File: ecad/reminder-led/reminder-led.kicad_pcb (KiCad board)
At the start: 2 copper layers, 13 parts, among them J1 MOLEX SL 1x5, Q1 2N3904, Q2 2N3904, Q3 2N3904

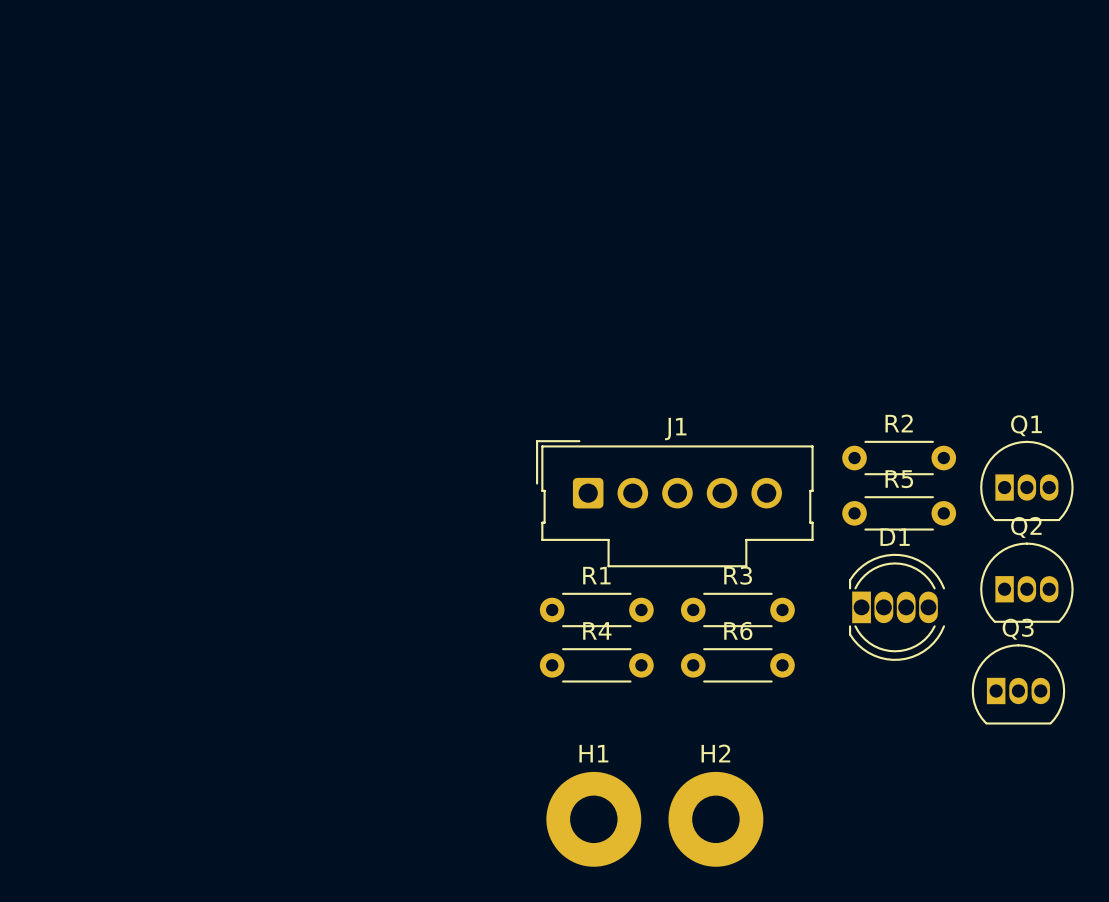
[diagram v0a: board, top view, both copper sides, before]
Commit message: Changed LED board type to 5050 LED
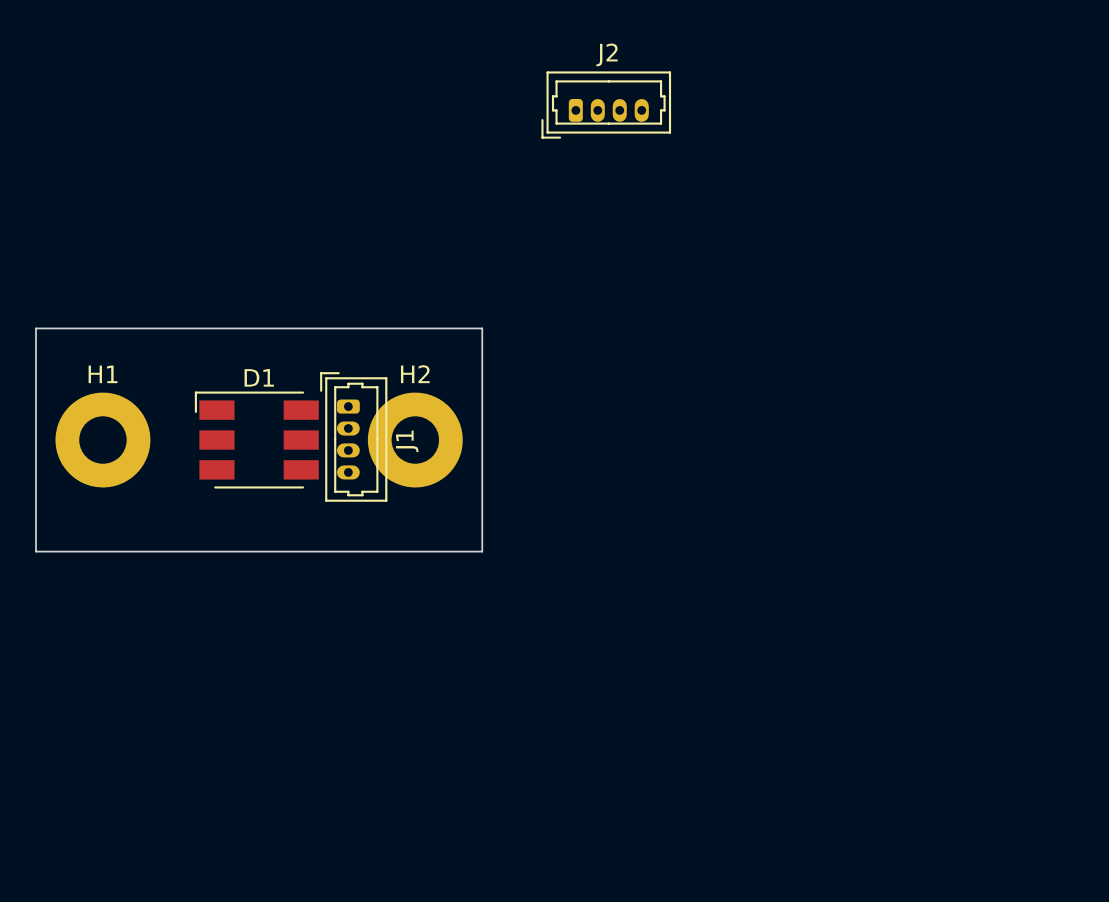
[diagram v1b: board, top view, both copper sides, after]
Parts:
- removed Q1, Q2, Q3: 2N3904, Package_TO_SOT_THT:TO-92_Inline
- removed R1, R2, R3: 620, Resistor_THT:R_Axial_DIN0204_L3.6mm_D1.6mm_P5.08mm_Horizontal
- removed R4: 130, Resistor_THT:R_Axial_DIN0204_L3.6mm_D1.6mm_P5.08mm_Horizontal
- removed R5, R6: 91, Resistor_THT:R_Axial_DIN0204_L3.6mm_D1.6mm_P5.08mm_Horizontal
- added J2: 0530470410, Connector_Molex:Molex_PicoBlade_53047-0410_1x04_P1.25mm_Vertical, F.Cu at (151.4, 70.1)
- D1: value LED_RGBA -> APA102; footprint LED_THT:LED_D5.0mm-4_RGB -> LED_SMD:LED_RGB_5050-6
- J1: value MOLEX SL 1x5 -> 0530470410; footprint Connector_Molex:Molex_SL_171971-0005_1x05_P2.54mm_Vertical -> Connector_Molex:Molex_PicoBlade_53047-0410_1x04_P1.25mm_Vertical
- moved D1 35.6 mm to (133.3, 88.9)
- moved H1 35.3 mm to (124.5, 88.9)
- moved H2 27.5 mm to (142.2, 88.9)
- moved J1 14.5 mm to (138.4, 87.0), turned to 270 degrees
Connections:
- D1 pad 1: Net-(D1-Pad1) -> /SER_IN
- D1 pad 2: Net-(D1-Pad2) -> /CLK_IN
- D1 pad 3: Net-(D1-Pad3) -> GND
- J1 pad 2: /LED_R -> /SER_IN
- J1 pad 3: /LED_G -> /CLK_IN
- J1 pad 4: /LED_B -> GND
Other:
- board outline added: 25.4 x 12.7 mm

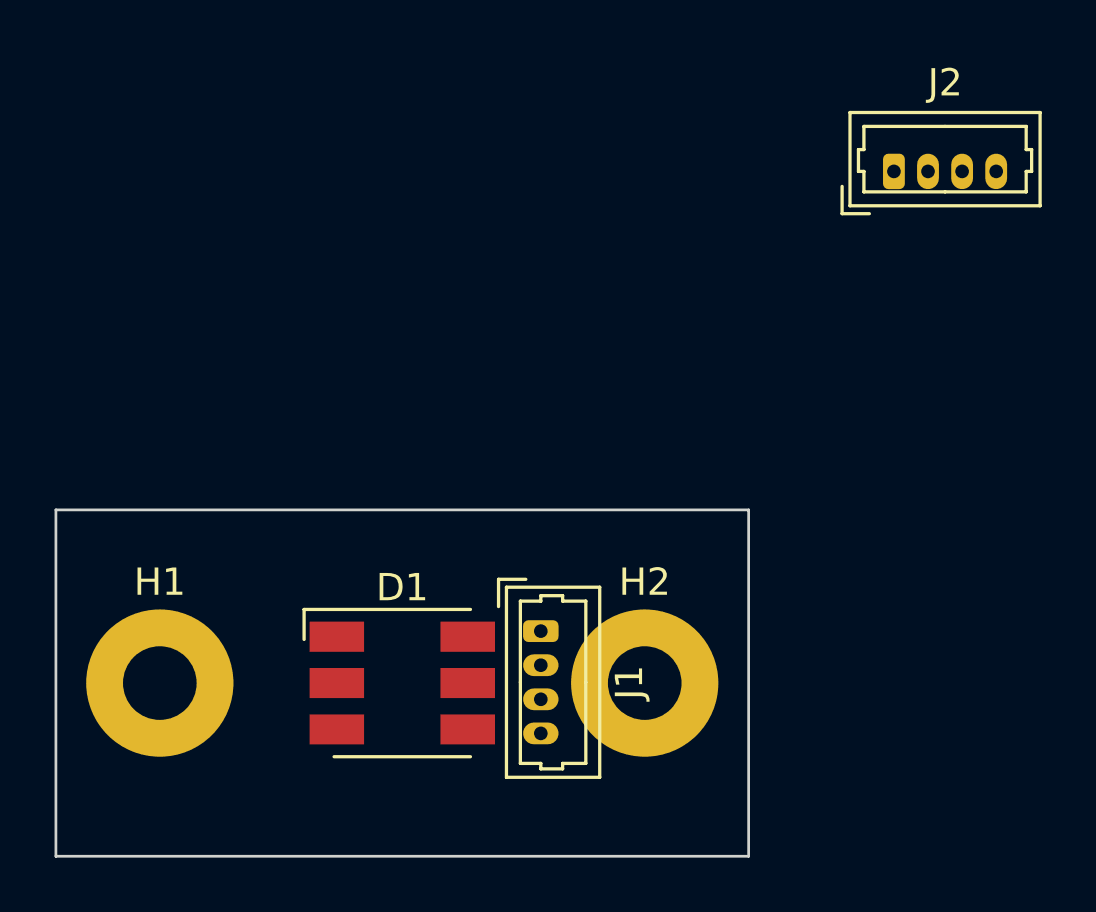
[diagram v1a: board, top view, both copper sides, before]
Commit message: Finished LED board routing and detailing
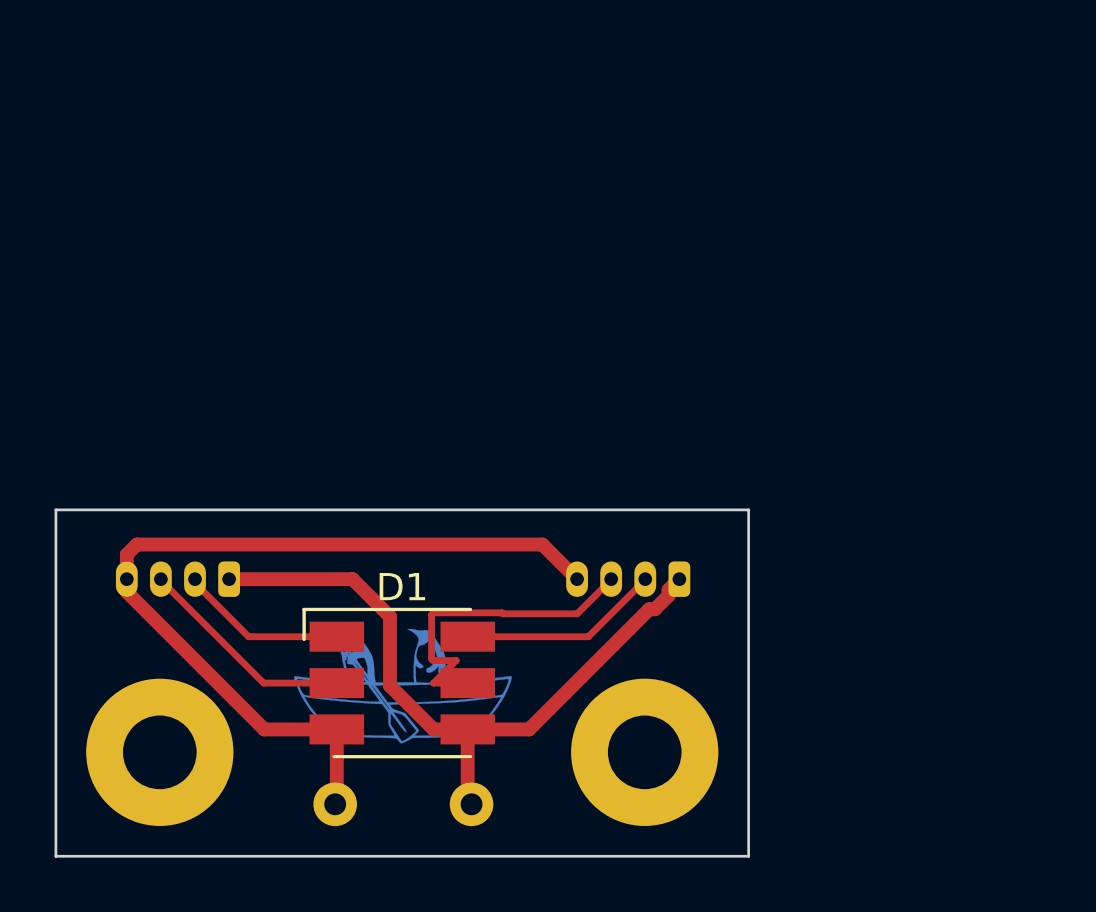
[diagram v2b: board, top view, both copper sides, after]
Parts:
- added C1: 10uF 10V, Capacitor_THT:C_Rect_L7.0mm_W2.0mm_P5.00mm, B.Cu at (135.9, 93.3)
- added G***: LOGO, Decals:8mm-penguin, B.Cu at (133.3, 88.9)
- J1, J2: moved to B.Cu
- moved J2 16.9 mm to (143.5, 85.1), turned to 180 degrees
- moved J1 11.6 mm to (127.0, 85.1), turned to 180 degrees
- moved H1 2.54 mm to (124.5, 91.4)
- moved H2 2.54 mm to (142.2, 91.4)
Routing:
- net GND: track 0.00 -> 31.1 mm
- net +5V: track 0.00 -> 25.5 mm
- net /CLK_OUT: track 0.00 -> 12.1 mm
- net /CLK_IN: track 0.00 -> 8.05 mm
- net /SER_OUT: track 0.00 -> 7.40 mm
- net /SER_IN: track 0.00 -> 6.16 mm
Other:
- board text added: "5V SER CLK GND"
- board text added: "IN"
- board text added: "OUT"

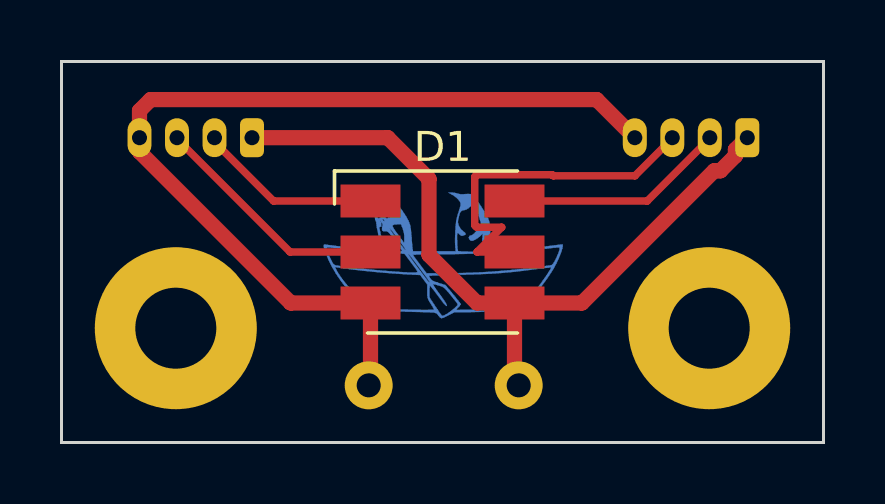
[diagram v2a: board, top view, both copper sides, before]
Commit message: Added rev text and chamfered corners of PCB
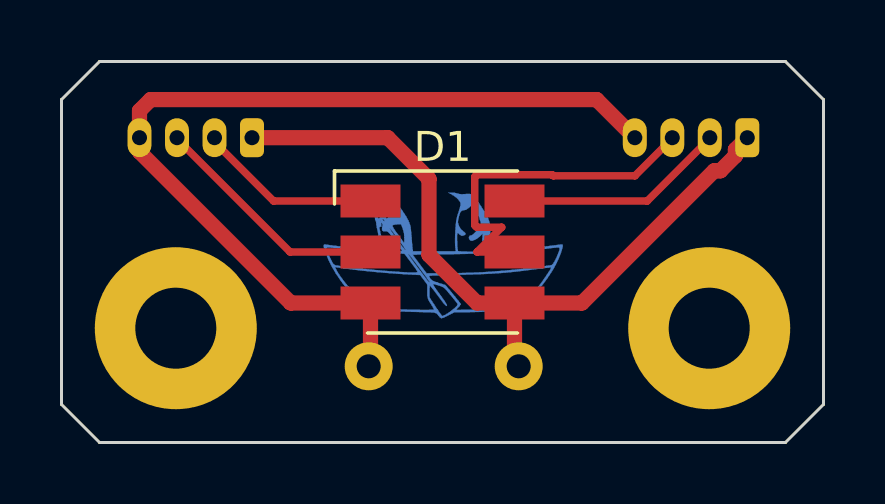
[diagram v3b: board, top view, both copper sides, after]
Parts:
- moved C1 0.64 mm to (135.9, 92.7)
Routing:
- net +5V: track 25.5 -> 24.9 mm
- net GND: track 31.1 -> 30.5 mm
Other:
- outline, holes or cut-outs redrawn
- board text added: "med-reminder LED revA - JDG 5.8.21"
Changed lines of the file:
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@@
   (general
     (thickness 1.6)
-    (drawings 11)
+    (drawings 16)
     (tracks 42)
     (zones 0)
@@
     (0 F.Cu signal)
     (31 B.Cu signal)
-    (32 B.Adhes user hide)
-    (33 F.Adhes user hide)
+    (32 B.Adhes user)
+    (33 F.Adhes user)
     (34 B.Paste user)
-    (35 F.Paste user hide)
+    (35 F.Paste user)
     (36 B.SilkS user)
-    (37 F.SilkS user hide)
+    (37 F.SilkS user)
     (38 B.Mask user)
-    (39 F.Mask user hide)
-    (40 Dwgs.User user hide)
-    (41 Cmts.User user hide)
-    (42 Eco1.User user hide)
-    (43 Eco2.User user hide)
+    (39 F.Mask user)
+    (40 Dwgs.User user)
+    (41 Cmts.User user)
+    (42 Eco1.User user)
+    (43 Eco2.User user)
     (44 Edge.Cuts user)
-    (45 Margin user hide)
+    (45 Margin user)
     (46 B.CrtYd user)
-    (47 F.CrtYd user hide)
+    (47 F.CrtYd user)
     (48 B.Fab user)
-    (49 F.Fab user hide)
+    (49 F.Fab user)
   )
   (setup
@@
   )
   (module Capacitor_THT:C_Rect_L7.0mm_W2.0mm_P5.00mm (layer B.Cu)
-    (at 135.89 93.345 180)
+    (at 135.89 92.71 180)
     (descr "C, Rect series, Radial, pin pitch=5.00mm, , length*width=7*2mm^2, Capacitor")
     (tags "C Rect series Radial pin pitch 5.00mm  length 7mm width 2mm Capacitor")
@@
     (pad 1 thru_hole circle (at 0 0) (size 5.4 5.4) (drill 2.7) (layers *.Cu *.Mask))
   )
+  (gr_text "med-reminder LED revA - JDG 5.8.21" (at 133.35 94.615) (layer B.SilkS)
+    (effects (font (size 0.508 0.508) (thickness 0.1016)) (justify mirror))
+  )
+  (gr_line (start 120.65 93.98) (end 120.65 83.82) (layer Edge.Cuts) (width 0.1))
+  (gr_line (start 144.78 95.25) (end 121.92 95.25) (layer Edge.Cuts) (width 0.1))
+  (gr_line (start 146.05 83.82) (end 146.05 93.98) (layer Edge.Cuts) (width 0.1))
+  (gr_line (start 121.92 82.55) (end 144.78 82.55) (layer Edge.Cuts) (width 0.1))
+  (gr_line (start 120.65 93.98) (end 121.92 95.25) (layer Edge.Cuts) (width 0.1))
+  (gr_line (start 120.65 83.82) (end 121.92 82.55) (layer Edge.Cuts) (width 0.1))
+  (gr_line (start 146.05 83.82) (end 144.78 82.55) (layer Edge.Cuts) (width 0.1))
+  (gr_line (start 144.78 95.25) (end 146.05 93.98) (layer Edge.Cuts) (width 0.1))
   (gr_text "5V SER CLK GND" (at 133.35 83.185) (layer B.SilkS)
     (effects (font (size 0.508 0.508) (thickness 0.1016)) (justify mirror))
@@
     (effects (font (size 1.5 1.5) (thickness 0.3)) (justify mirror))
   )
-  (gr_line (start 120.65 95.25) (end 120.65 82.55) (layer Edge.Cuts) (width 0.1))
-  (gr_line (start 146.05 95.25) (end 120.65 95.25) (layer Edge.Cuts) (width 0.1))
-  (gr_line (start 146.05 82.55) (end 146.05 95.25) (layer Edge.Cuts) (width 0.1))
-  (gr_line (start 120.65 82.55) (end 146.05 82.55) (layer Edge.Cuts) (width 0.1))
   (segment (start 134.5 90.6) (end 135.75 90.6) (width 0.508) (layer F.Cu) (net 1))
   (segment (start 132.89999 88.99999) (end 134.5 90.6) (width 0.508) (layer F.Cu) (net 1))
@@
   (segment (start 138 90.6) (end 135.75 90.6) (width 0.508) (layer F.Cu) (net 1))
   (segment (start 143.51 85.09) (end 143.11401 85.48599) (width 0.508) (layer F.Cu) (net 1))
-  (segment (start 135.75 93.205) (end 135.89 93.345) (width 0.508) (layer F.Cu) (net 1))
-  (segment (start 135.75 90.6) (end 135.75 93.205) (width 0.508) (layer F.Cu) (net 1))
+  (segment (start 135.75 92.57) (end 135.89 92.71) (width 0.25) (layer F.Cu) (net 1))
+  (segment (start 135.75 90.6) (end 135.75 92.57) (width 0.508) (layer F.Cu) (net 1))
   (segment (start 123.25 85.558845) (end 128.291155 90.6) (width 0.508) (layer F.Cu) (net 2))
   (segment (start 123.25 85.09) (end 123.25 85.558845) (width 0.508) (layer F.Cu) (net 2))
@@
   (segment (start 123.25 84.19) (end 123.62 83.82) (width 0.508) (layer F.Cu) (net 2))
   (segment (start 123.25 85.09) (end 123.25 84.19) (width 0.508) (layer F.Cu) (net 2))
-  (segment (start 130.95 93.285) (end 130.89 93.345) (width 0.508) (layer F.Cu) (net 2))
-  (segment (start 130.95 90.6) (end 130.95 93.285) (width 0.508) (layer F.Cu) (net 2))
+  (segment (start 130.95 92.65) (end 130.89 92.71) (width 0.25) (layer F.Cu) (net 2))
+  (segment (start 130.95 90.6) (end 130.95 92.65) (width 0.508) (layer F.Cu) (net 2))
   (segment (start 142.26 85.115318) (end 142.26 85.09) (width 0.25) (layer F.Cu) (net 3))
   (segment (start 140.175318 87.2) (end 142.26 85.115318) (width 0.25) (layer F.Cu) (net 3))

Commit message: Finished mainboard schematic layout
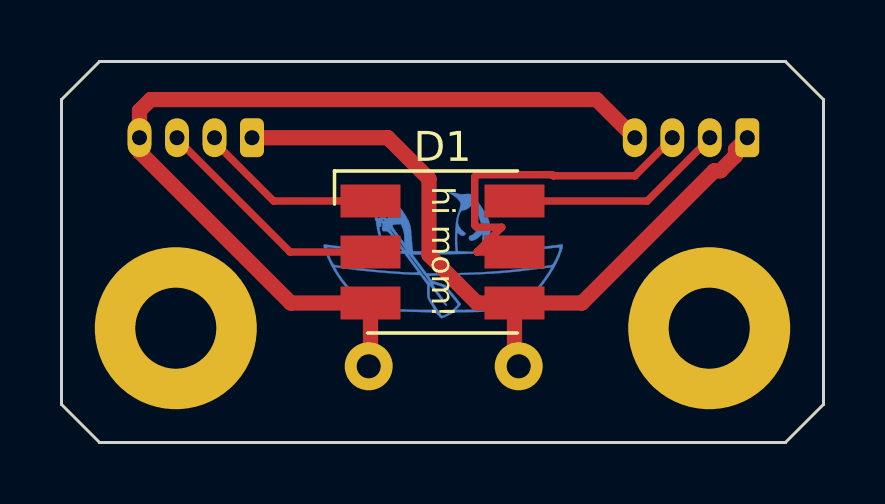
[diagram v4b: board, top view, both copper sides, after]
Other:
- board text added: "hi mom!"
